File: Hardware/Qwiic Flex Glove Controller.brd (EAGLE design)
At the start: 25.4 x 36.8 mm, 43 parts, among them U1 ADS1015, U4 LMV358

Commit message: cleaned repo
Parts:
- moved U$14 48.8 mm to (24.4, 14.0), flipped to the bottom
- moved U$3 48.5 mm to (24.3, 18.4), flipped to the bottom
- moved U$4 48.5 mm to (24.3, 21.0), flipped to the bottom
- moved C1 46.5 mm to (23.2, 6.35), flipped to the top
- moved R6 45.7 mm to (22.9, 12.2), flipped to the top
- moved JP2 44.5 mm to (22.2, 22.9), flipped to the bottom
- moved JP3 44.5 mm to (22.2, 20.3), flipped to the bottom
- moved FD1 43.7 mm to (21.8, 5.08), flipped to the top
- moved FD2 43.7 mm to (21.8, 5.08), flipped to the bottom
- moved LOGO3 43.7 mm to (21.8, 0.38), flipped to the top
- moved U$10 40.6 mm to (20.3, 2.03), flipped to the bottom
- moved U$9 40.6 mm to (20.3, 2.03), flipped to the top
- moved U$12 40.4 mm to (20.2, 21.0), flipped to the bottom
- moved U$13 40.4 mm to (20.2, 18.3), flipped to the bottom
- moved LOGO1 37.1 mm to (18.5, 15.2), flipped to the bottom
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
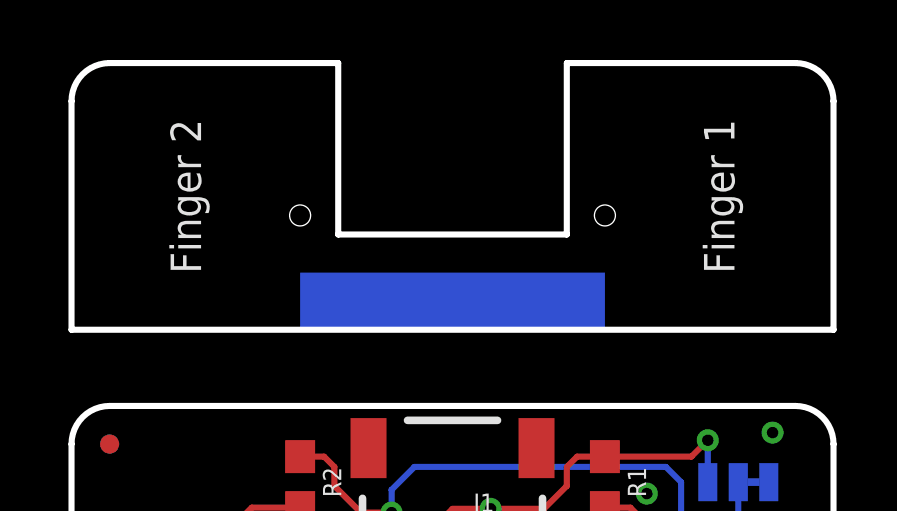
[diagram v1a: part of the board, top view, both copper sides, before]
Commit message: added buzzard finger labels
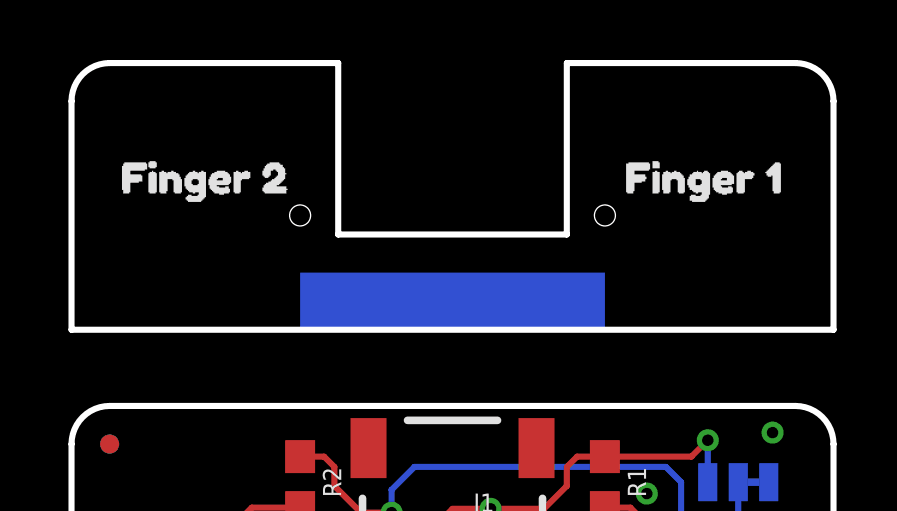
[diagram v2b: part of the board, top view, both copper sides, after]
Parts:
- added U$16: (no value), buzzard_labels (6):FINGER_10
- added U$17: (no value), buzzard_labels (6):FINGER_21
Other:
- board text removed: "Finger 1"
- board text removed: "Finger 2"
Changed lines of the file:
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@@
 <rectangle x1="7.62" y1="15.24" x2="17.78" y2="18.415" layer="29"/>
 <rectangle x1="7.239" y1="14.859" x2="18.161" y2="18.923" layer="31"/>
-<text x="21.59" y="32.385" size="1.016" layer="21" font="vector" ratio="15" rot="R90" align="center">Finger 1</text>
-<text x="3.81" y="32.385" size="1.016" layer="21" font="vector" ratio="15" rot="R90" align="center">Finger 2</text>
 <wire x1="19.05" y1="16.51" x2="25.4" y2="16.51" width="0.2032" layer="21"/>
 <dimension x1="0" y1="27.94" x2="25.4" y2="27.94" x3="12.7" y3="39.37" textsize="1.778" layer="47" unit="inch"/>
@@
 <element name="TP2" library="SparkFun-Connectors" package="PAD.03X.03" value="TEST-POINT3" x="7.62" y="10.16" rot="MR0"/>
 <element name="U$14" library="buzzard_labels (5)" package="QWIIC_FLEX_GLOVE0" value="" x="24.384" y="13.97" rot="MR0"/>
+<element name="U$16" library="buzzard_labels (6)" package="FINGER_10" value="" x="17.526" y="33.02"/>
+<element name="U$17" library="buzzard_labels (6)" package="FINGER_21" value="" x="0.762" y="33.02"/>
 </elements>
 <signals>

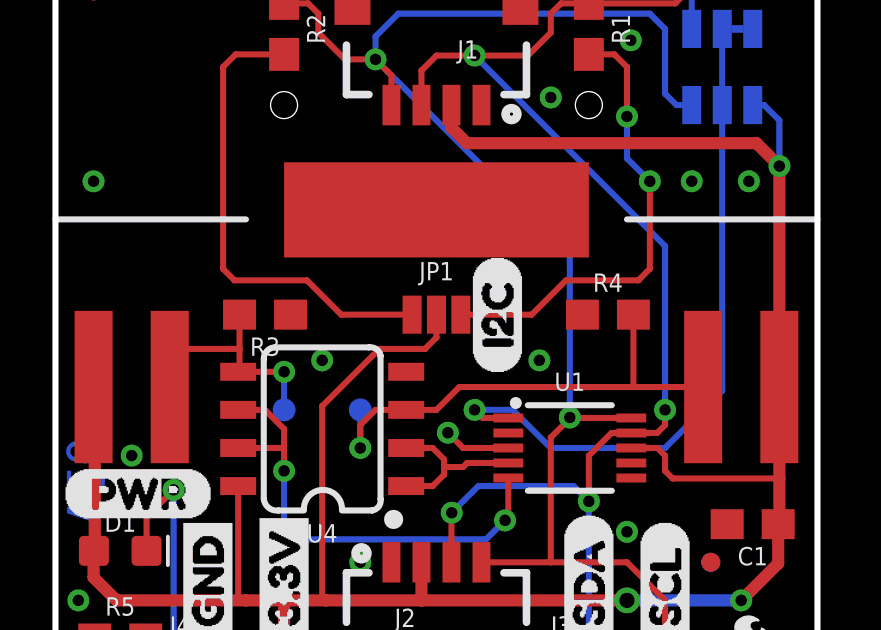
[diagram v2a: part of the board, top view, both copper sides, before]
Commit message: changed to Trace Jumper
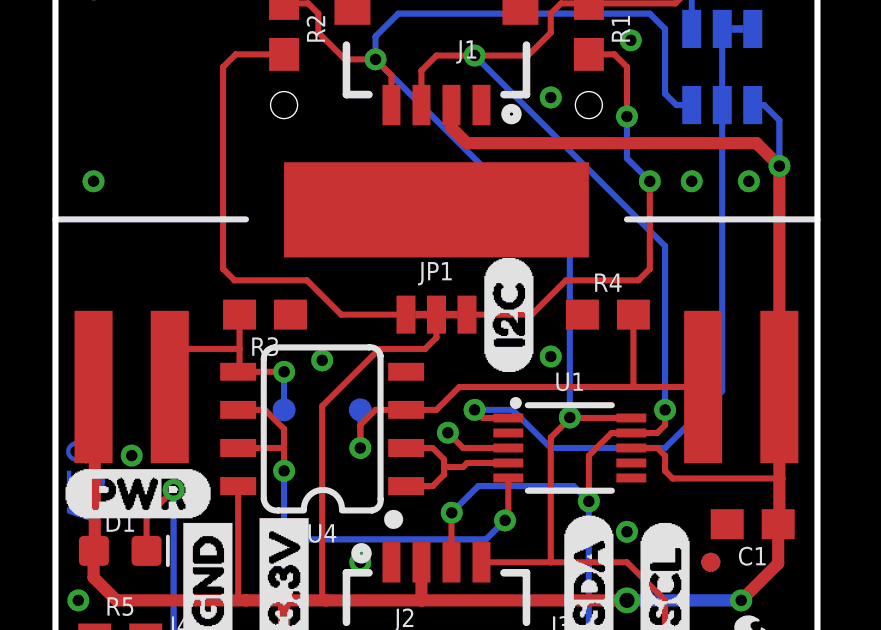
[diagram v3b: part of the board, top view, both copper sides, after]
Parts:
- JP1: value JUMPER-SMT_3_2-NC_PASTE_NO-SILK -> JUMPER-SMT_3_2-NC_TRACE_NO-SILK; device SparkFun-Jumpers:SMT-JUMPER_3_2-NC_PASTE_NO-SILK -> SparkFun-Jumpers:SMT-JUMPER_3_2-NC_TRACE_NO-SILK
- moved U$15 0.38 mm to (15.1, 11.3)
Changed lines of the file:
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@@
 <layer number="29" name="tStop" color="7" fill="3" visible="no" active="yes"/>
 <layer number="30" name="bStop" color="7" fill="6" visible="no" active="yes"/>
-<layer number="31" name="tCream" color="7" fill="4" visible="no" active="yes"/>
+<layer number="31" name="tCream" color="7" fill="4" visible="yes" active="yes"/>
 <layer number="32" name="bCream" color="7" fill="5" visible="no" active="yes"/>
 <layer number="33" name="tFinish" color="6" fill="3" visible="no" active="yes"/>
@@
 <attribute name="PROD_ID" value="RES-07857" x="7.62" y="22.86" size="1.778" layer="27" rot="R270" display="off"/>
 </element>
-<element name="JP1" library="SparkFun-Jumpers" package="SMT-JUMPER_3_2-NC_PASTE_NO-SILK" value="JUMPER-SMT_3_2-NC_PASTE_NO-SILK" x="12.7" y="13.335"/>
+<element name="JP1" library="SparkFun-Jumpers" package="SMT-JUMPER_3_2-NC_TRACE_NO-SILK" value="JUMPER-SMT_3_2-NC_TRACE_NO-SILK" x="12.7" y="13.335"/>
 <element name="J2" library="SparkFun-Connectors" package="1X04_1MM_RA" value="" x="12.7" y="5.08">
 <attribute name="PROD_ID" value="CONN-13694" x="3.81" y="15.24" size="1.778" layer="27" display="off"/>
@@
 <element name="U$12" library="buzzard_labels (3)" package="SDA0" value="" x="20.193" y="20.955" rot="MR90"/>
 <element name="U$13" library="buzzard_labels (4)" package="SCL2" value="" x="20.193" y="18.288" rot="MR90"/>
-<element name="U$15" library="Labels" package="I2C-()" value="" x="14.732" y="11.303" rot="R90"/>
+<element name="U$15" library="Labels" package="I2C-()" value="" x="15.113" y="11.303" rot="R90"/>
 <element name="TP1" library="SparkFun-Connectors" package="PAD.03X.03" value="TEST-POINT3" x="10.16" y="10.16" rot="MR0"/>
 <element name="TP2" library="SparkFun-Connectors" package="PAD.03X.03" value="TEST-POINT3" x="7.62" y="10.16" rot="MR0"/>
@@
 </polygon>
 <contactref element="J2" pad="1"/>
-<via x="16.129" y="11.811" extent="1-16" drill="0.381"/>
+<via x="16.51" y="11.938" extent="1-16" drill="0.381"/>
 <via x="2.54" y="8.636" extent="1-16" drill="0.381"/>
 <via x="1.27" y="17.78" extent="1-16" drill="0.381"/>
@@
 <contactref element="JP1" pad="1"/>
 <contactref element="R2" pad="2"/>
-<wire x1="11.8872" y1="13.335" x2="9.525" y2="13.335" width="0.2032" layer="1"/>
+<wire x1="11.684" y1="13.335" x2="9.525" y2="13.335" width="0.2032" layer="1"/>
 <wire x1="9.525" y1="13.335" x2="8.382" y2="14.478" width="0.2032" layer="1"/>
 <wire x1="8.382" y1="14.478" x2="5.969" y2="14.478" width="0.2032" layer="1"/>
@@
 <contactref element="JP1" pad="3"/>
 <contactref element="R1" pad="2"/>
-<wire x1="13.5128" y1="13.335" x2="15.875" y2="13.335" width="0.2032" layer="1"/>
+<wire x1="13.716" y1="13.335" x2="15.875" y2="13.335" width="0.2032" layer="1"/>
 <wire x1="15.875" y1="13.335" x2="17.018" y2="14.478" width="0.2032" layer="1"/>
 <wire x1="17.018" y1="14.478" x2="19.431" y2="14.478" width="0.2032" layer="1"/>

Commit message: Added panel
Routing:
- net VCC: track 85.9 -> 87.9 mm
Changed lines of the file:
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@@
 <wire x1="24.13" y1="18.288" x2="24.13" y2="10.922" width="0.4064" layer="1"/>
 <contactref element="R7" pad="P$1"/>
-<wire x1="1.309" y1="12.153" x2="1.27" y2="10.922" width="0" layer="19" extent="1-1"/>
+<wire x1="1.309" y1="12.153" x2="1.27" y2="12.153" width="0.4064" layer="1"/>
+<wire x1="1.27" y1="12.153" x2="1.27" y2="10.922" width="0.4064" layer="1"/>
+<wire x1="1.27" y1="10.922" x2="1.27" y2="10.16" width="0.4064" layer="1"/>
 </signal>
 <signal name="GND">
